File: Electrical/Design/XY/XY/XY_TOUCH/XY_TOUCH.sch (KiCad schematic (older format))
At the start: 346 parts, among them J1 Conn_01x06, J2 Conn_01x10, U1 MXT144U

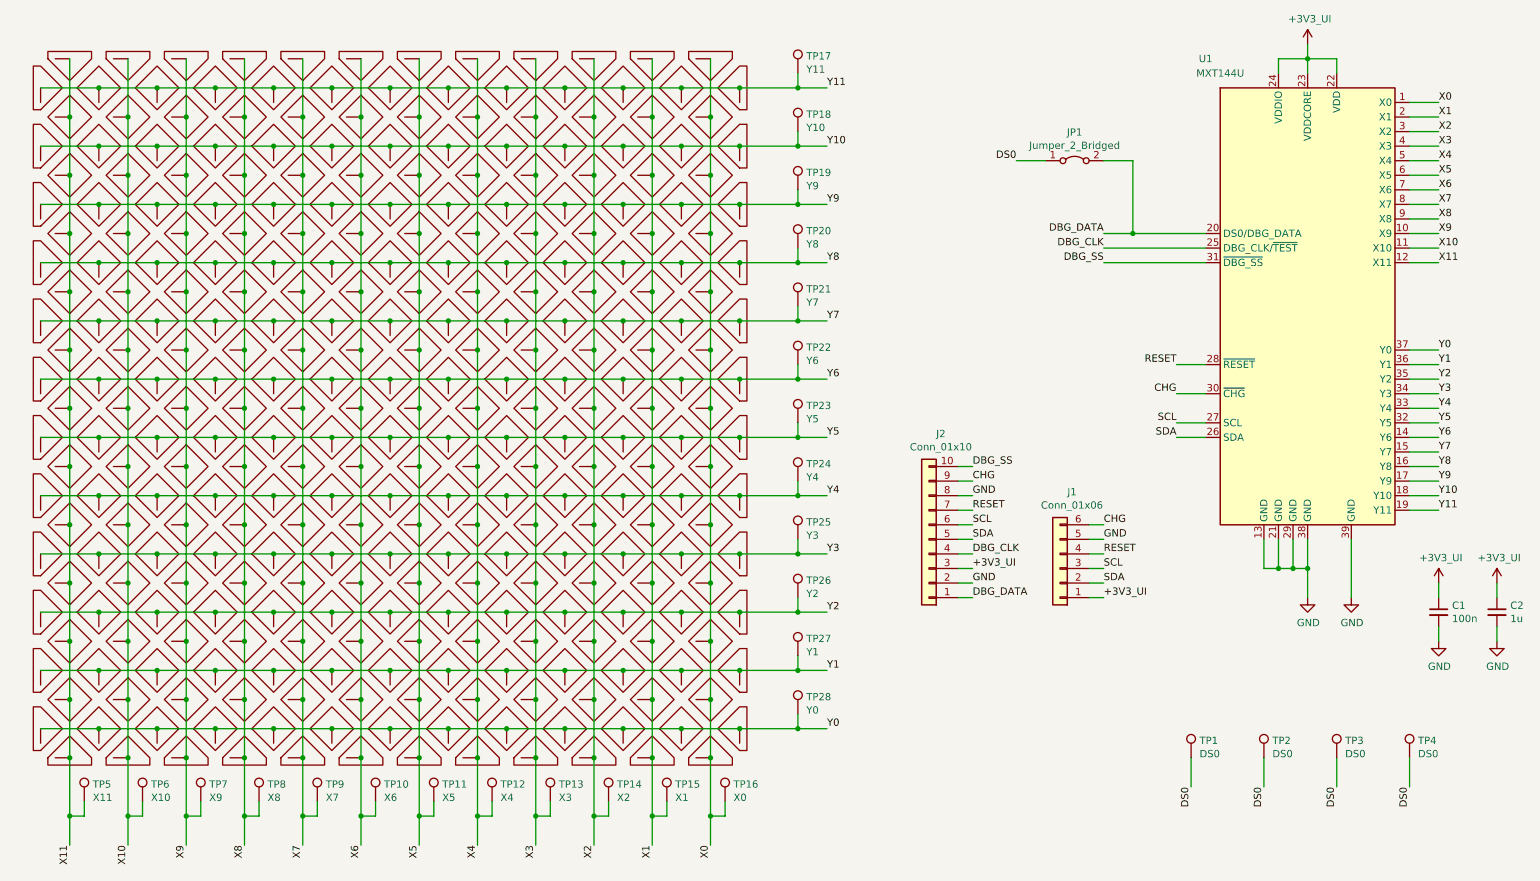
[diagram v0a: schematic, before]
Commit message: SUKU pcb gerber ordered
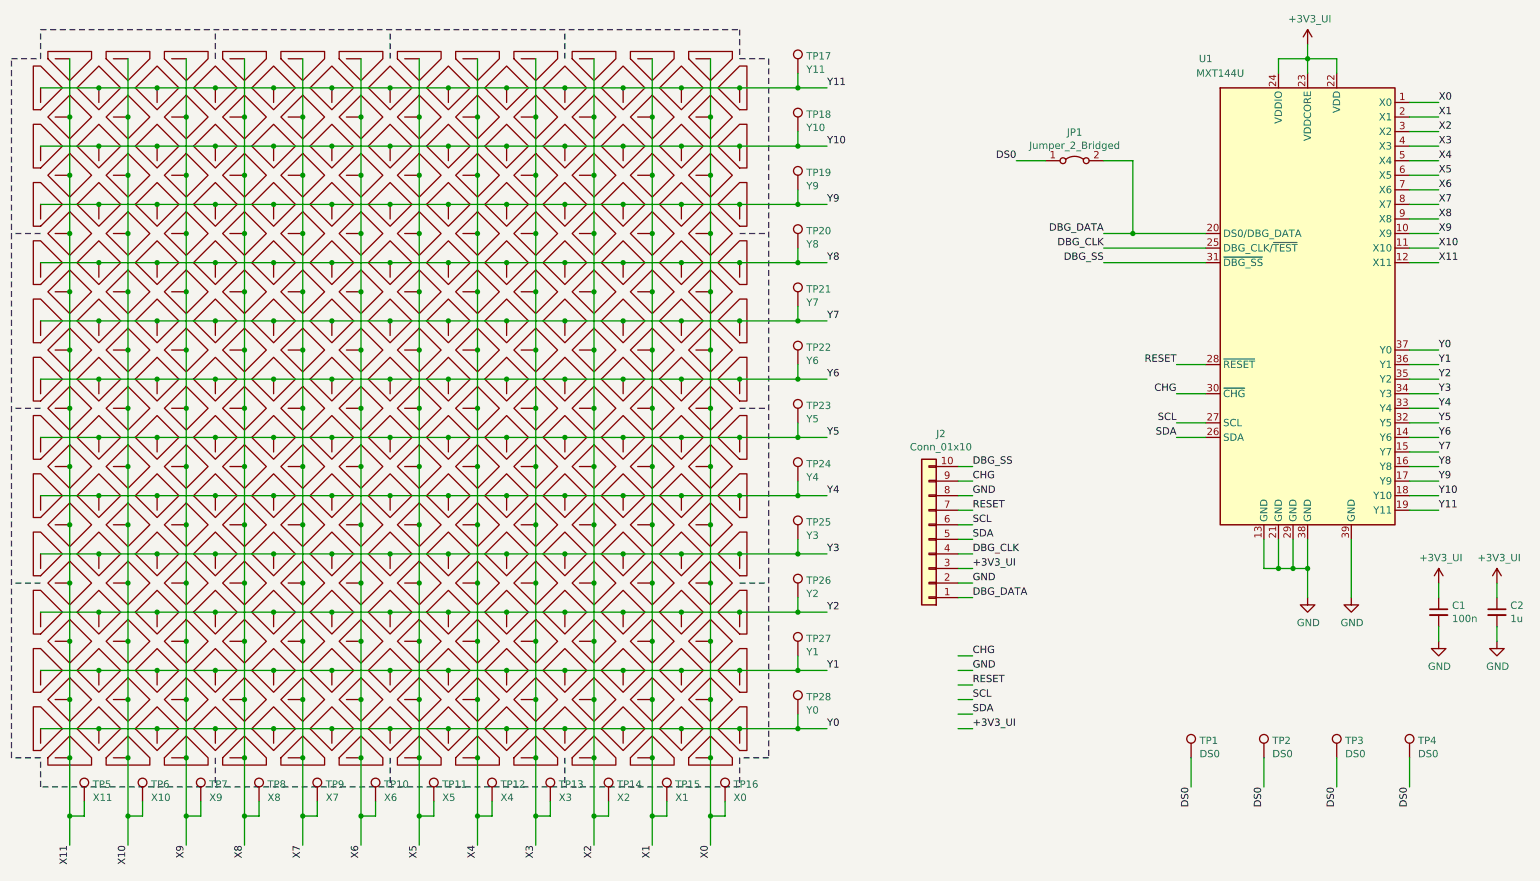
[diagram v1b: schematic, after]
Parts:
- removed J1: Conn_01x06, Connector_FFC-FPC:Molex_200528-0060_1x06-1MP_P1.00mm_Horizontal, symbol Connector_Generic:Conn_01x06
- CS1, CS10, CS100, CS138, CS175, CS213, CS25, CS250, CS288, CS303, CS306, CS309, CS312, CS4, CS63, CS7: footprint suku_basics:capsense_diamond_edge -> suku_basics:capsense_diamond_edge_bite_left
- CS12, CS13, CS150, CS163, CS225, CS238, CS3, CS300, CS301, CS304, CS307, CS310, CS6, CS75, CS88, CS9: footprint suku_basics:capsense_diamond_edge -> suku_basics:capsense_diamond_edge_bite_right
- CS141, CS144, CS147, CS151, CS153, CS154, CS156, CS157, CS159, CS16, CS160, CS162, CS166, CS169, CS172, CS19, CS216, CS219, CS22, CS222, CS226, CS228, CS229, CS231, CS232, CS234, CS235, CS237, CS241, CS244, CS247, CS291, CS294, CS297, CS66, CS69, CS72, CS76, CS78, CS79, CS81, CS82, CS84, CS85, CS87, CS91, CS94, CS97: footprint suku_basics:capsense_diamond -> suku_basics:capsense_diamond_bite
